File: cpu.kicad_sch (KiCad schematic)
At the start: 24 parts, among them U1 Z80CPU, U10 74HC00, U11 74HC138, U6 NE555D, U7 74HC04, Y1 Crystal

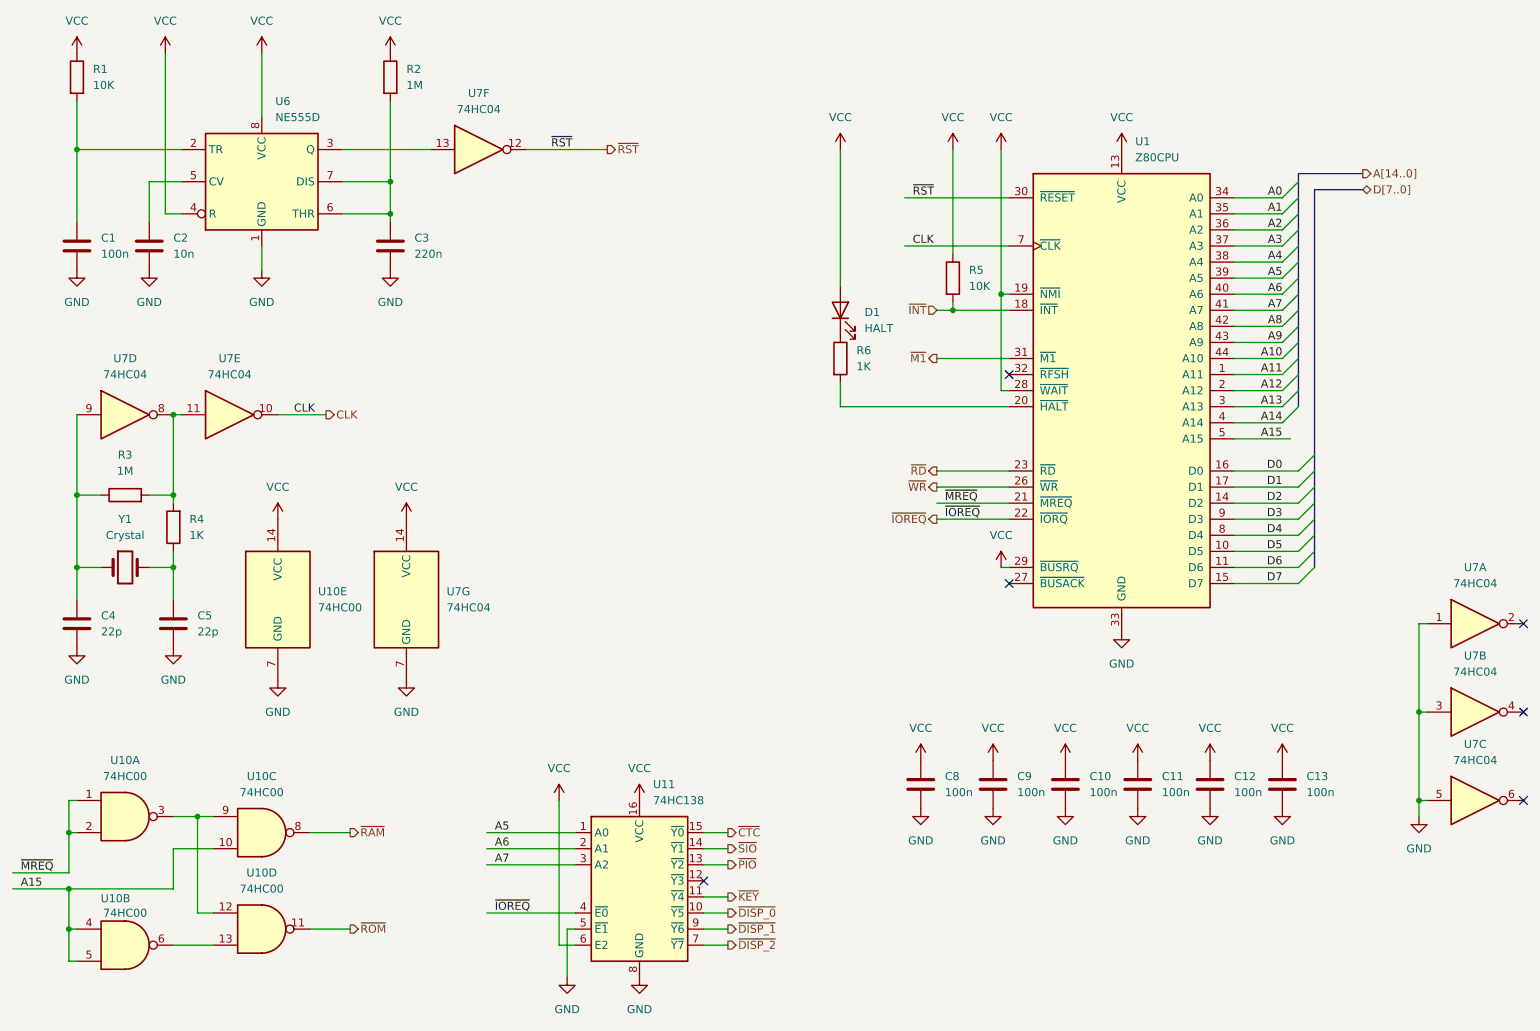
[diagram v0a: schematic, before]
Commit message: HW: Initial placement of I/O chips
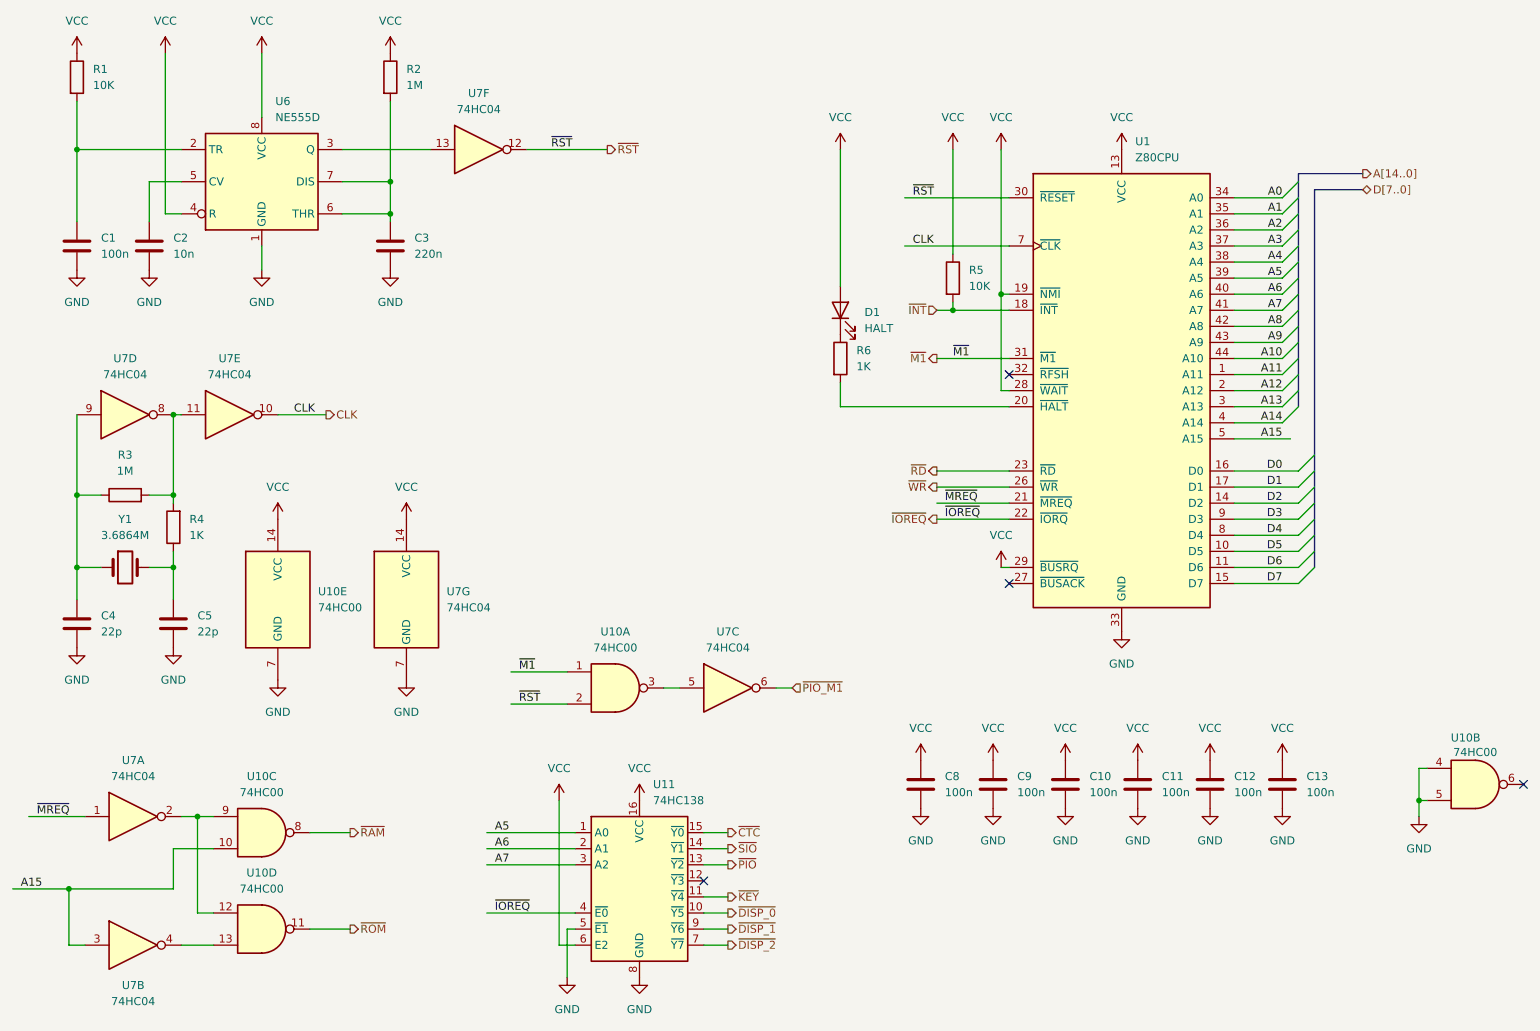
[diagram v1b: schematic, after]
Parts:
- Y1: value Crystal -> 3.6864M
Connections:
- net A15: now also U7.3; no longer U10.4, U10.5
- net GND: now also U10.4, U10.5; no longer U7.1, U7.3, U7.5
- net ~{M1}: now also U10.1
- net ~{MREQ}: now also U7.1; no longer U10.1, U10.2
- net ~{RST}: now also U10.2
- net at U10.12, U10.9: now also U7.2; no longer U10.3
- net ~{PIO_M1}: now reaches U7.6
- net at U7.4: now also U10.13
- net at U10.6: no longer U10.13
- new net: U10.3, U7.5
- no-connect marks 6 -> 4
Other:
- moved on the sheet: U10A, U10B, U7A, U7B, U7C

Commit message: HW: Update schematic info frames
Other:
- company: (none) -> A.K.
- title: (none) -> CPU, basics and glue logic
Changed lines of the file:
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@@
 	(generator_version "9.0")
 	(paper "A4")
+	(title_block
+		(title "CPU, basics and glue logic")
+		(date "2025-10-14")
+		(rev "A")
+		(company "A.K.")
+	)
 	(junction
 		(at 173.99 73.66)

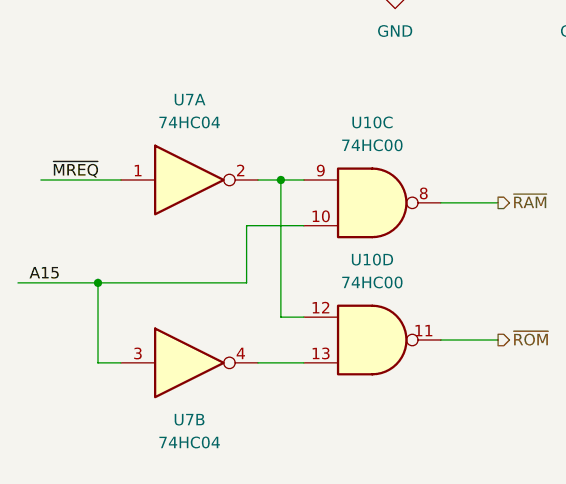
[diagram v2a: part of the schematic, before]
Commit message: HW: Add display, start PCB placement
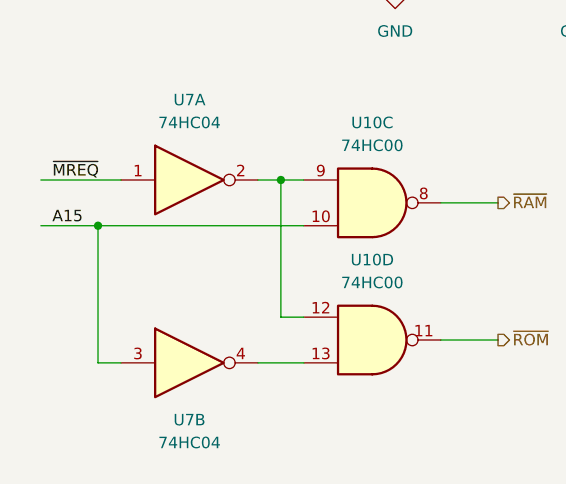
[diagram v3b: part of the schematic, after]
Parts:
- Y1: footprint (none) -> Crystal:Crystal_SMD_HC49-SD
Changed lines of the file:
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@@
 	)
 	(junction
-		(at 34.29 165.1)
-		(diameter 0)
-		(color 0 0 0 0)
-	)
-	(junction
 		(at 181.61 71.12)
 		(diameter 0)
@@
 	)
 	(junction
+		(at 34.29 158.75)
+		(diameter 0)
+		(color 0 0 0 0)
+	)
+	(junction
 		(at 35.56 114.3)
 		(diameter 0)
@@
 	(wire
 		(pts
-			(xy 50.8 158.75) (xy 57.15 158.75)
-		)
-		(stroke
-			(width 0)
-			(type default)
-		)
-	)
-	(wire
-		(pts
 			(xy 52.07 58.42) (xy 49.53 58.42)
 		)
@@
 		)
 	)
-	(wire
-		(pts
-			(xy 25.4 165.1) (xy 34.29 165.1)
-		)
-		(stroke
-			(width 0)
-			(type default)
-		)
-	)
 	(bus
 		(pts
@@
 	(wire
 		(pts
-			(xy 34.29 173.99) (xy 34.29 165.1)
-		)
-		(stroke
-			(width 0)
-			(type default)
-		)
-	)
-	(wire
-		(pts
 			(xy 54.61 153.67) (xy 57.15 153.67)
 		)
@@
 		)
 	)
-	(wire
+	(bus
 		(pts
-			(xy 34.29 165.1) (xy 50.8 165.1)
+			(xy 228.6 60.96) (xy 228.6 58.42)
 		)
 		(stroke
@@
 		)
 	)
-	(bus
+	(wire
 		(pts
-			(xy 228.6 60.96) (xy 228.6 58.42)
+			(xy 171.45 73.66) (xy 173.99 73.66)
 		)
 		(stroke
@@
 	(wire
 		(pts
-			(xy 171.45 73.66) (xy 173.99 73.66)
+			(xy 166.37 55.88) (xy 182.88 55.88)
 		)
 		(stroke
@@
 	(wire
 		(pts
-			(xy 166.37 55.88) (xy 182.88 55.88)
+			(xy 218.44 104.14) (xy 228.6 104.14)
 		)
 		(stroke
@@
 	(wire
 		(pts
-			(xy 50.8 165.1) (xy 50.8 158.75)
+			(xy 34.29 158.75) (xy 34.29 173.99)
 		)
 		(stroke
@@
 	(wire
 		(pts
-			(xy 218.44 104.14) (xy 228.6 104.14)
+			(xy 50.8 102.87) (xy 50.8 104.14)
 		)
 		(stroke
@@
 	(wire
 		(pts
-			(xy 50.8 102.87) (xy 50.8 104.14)
+			(xy 27.94 158.75) (xy 34.29 158.75)
 		)
 		(stroke
@@
 	(wire
 		(pts
+			(xy 34.29 158.75) (xy 57.15 158.75)
+		)
+		(stroke
+			(width 0)
+			(type default)
+		)
+	)
+	(wire
+		(pts
 			(xy 46.99 53.34) (xy 46.99 59.69)
 		)
@@
 	)
 	(label "A15"
-		(at 26.67 165.1 0)
+		(at 29.21 158.75 0)
 		(effects
 			(font
@@
 			)
 		)
-		(property "Footprint" ""
+		(property "Footprint" "Crystal:Crystal_SMD_HC49-SD"
 			(at 43.18 114.3 0)
 			(effects

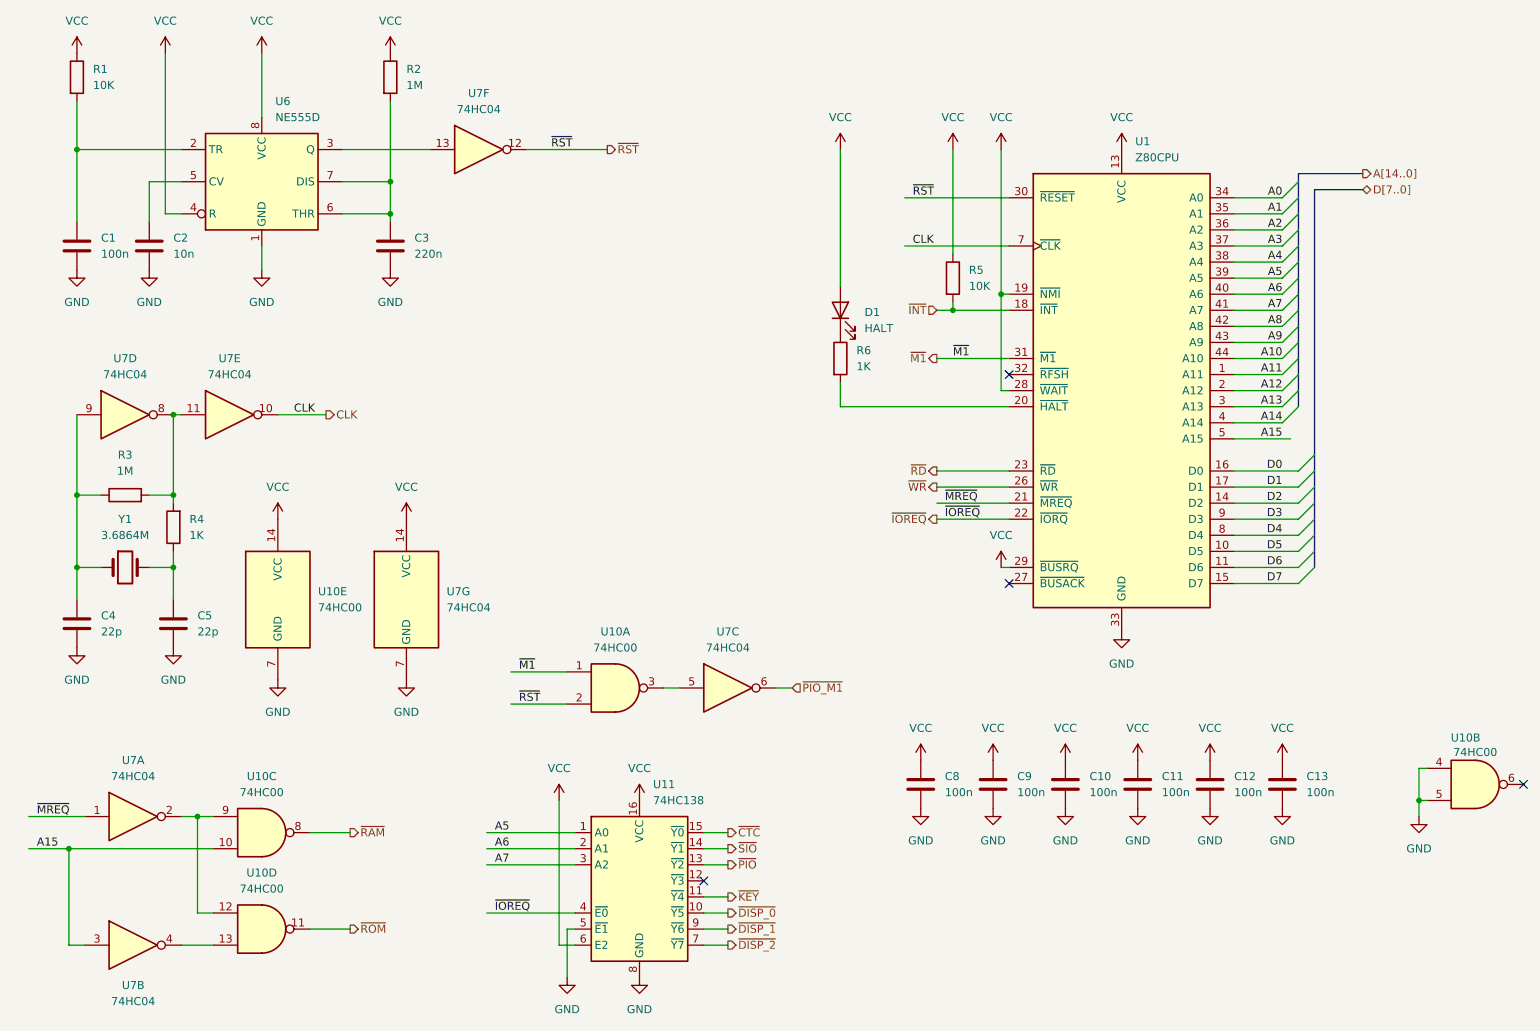
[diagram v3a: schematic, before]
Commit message: HW: Add rst button, sync pins
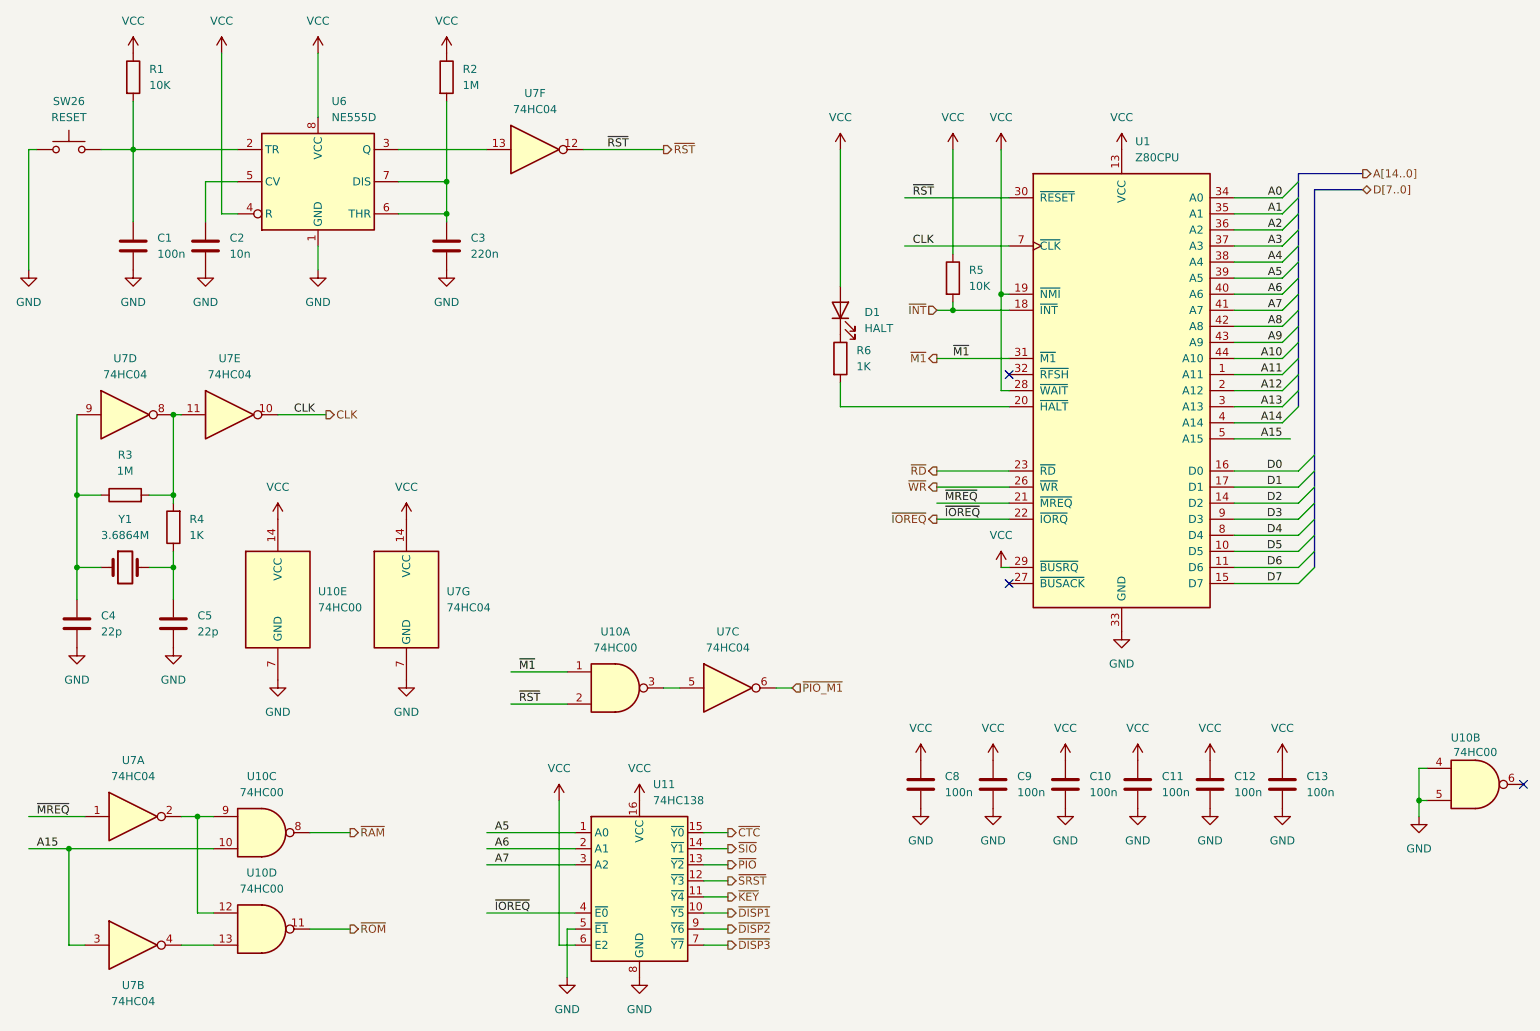
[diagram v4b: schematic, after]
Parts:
- added SW26: RESET, Button_Switch_SMD:SW_SPST_PTS645, symbol Switch:SW_Omron_B3FS
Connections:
- net GND: now also SW26.1
- net at C1.1, R1.2, U6.2 (TR): now also SW26.2
- net ~{SRST}: now reaches U11.12 (~{Y3})
- net ~{DISP_0} renamed ~{DISP1}
- net ~{DISP_1} renamed ~{DISP2}
- net ~{DISP_2} renamed ~{DISP3}
- no-connect marks 4 -> 3
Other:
- moved on the sheet: C1, C2, C3, R1, R2, U6, U7F
